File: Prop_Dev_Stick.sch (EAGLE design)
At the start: 54 parts, among them J1 MF-CON-MICROUSB-RIGHT, J3 M20-7822046, J4 M20-7822046, J5 M20-7820442, J6 M20-7820442, U1 P8X32A-Q44, U2 FT230XQ-R, U3 TPS2113ADRBR, U4 CAT24C512WI-GT3, U5 AD7999YRJZ-1500RL7, U6 TS2937CW33, U7 IRLML6401TRPBF, X1 ATS060CSM-1

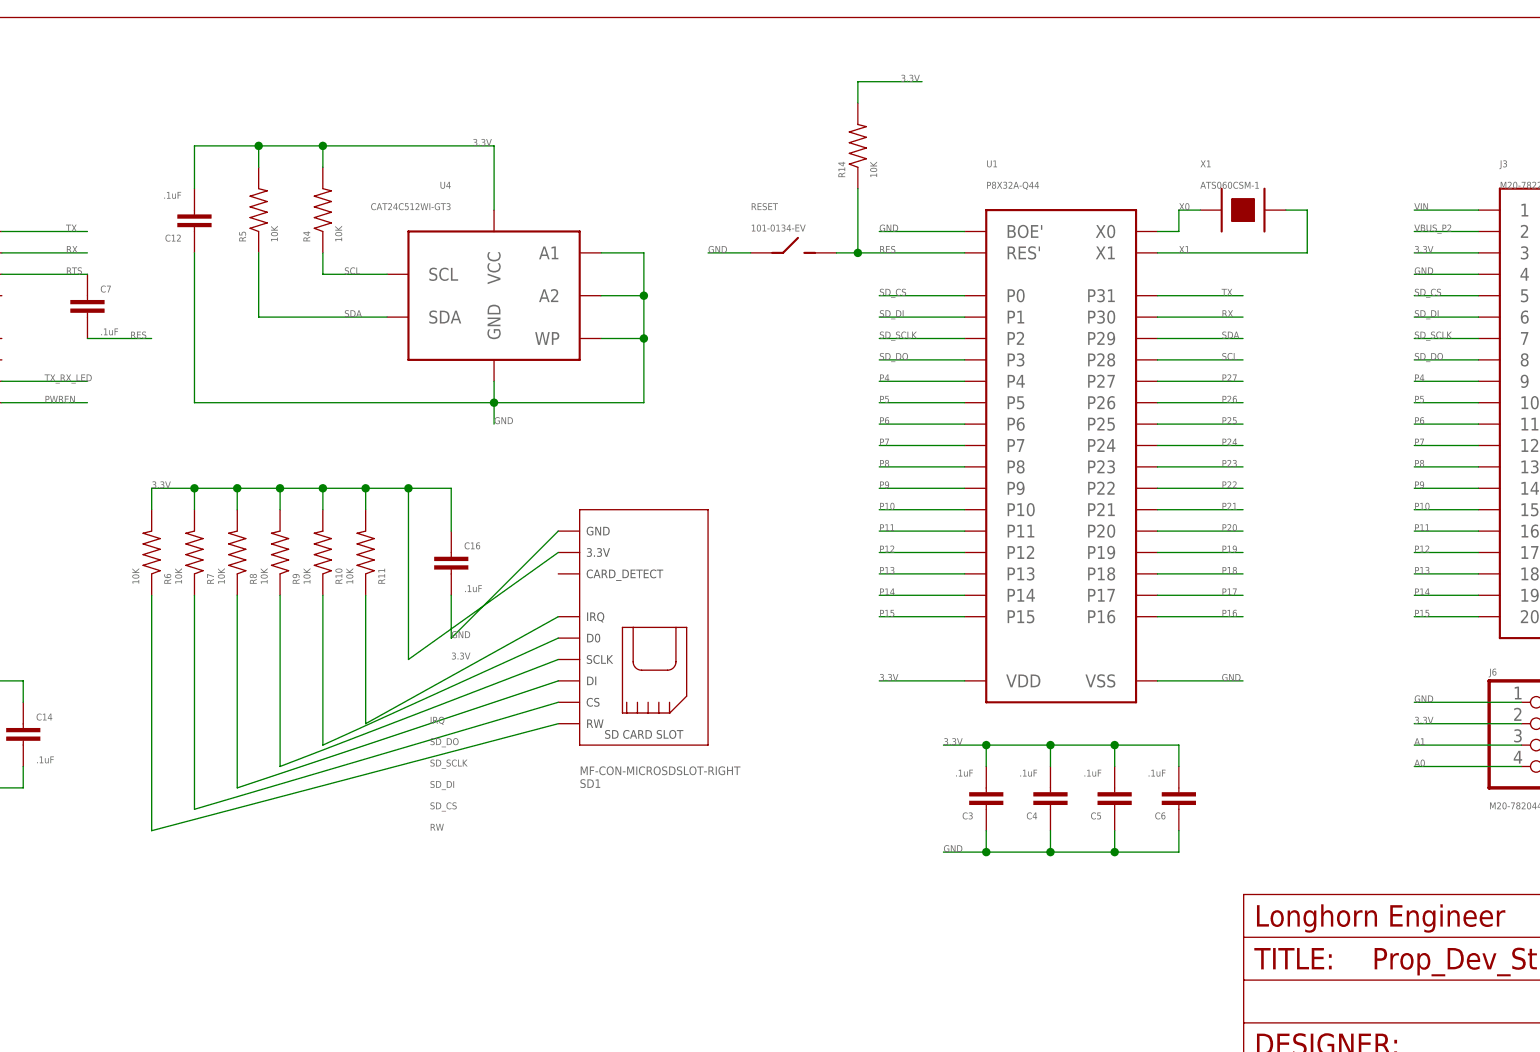
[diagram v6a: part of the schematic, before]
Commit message: Changed crystal.
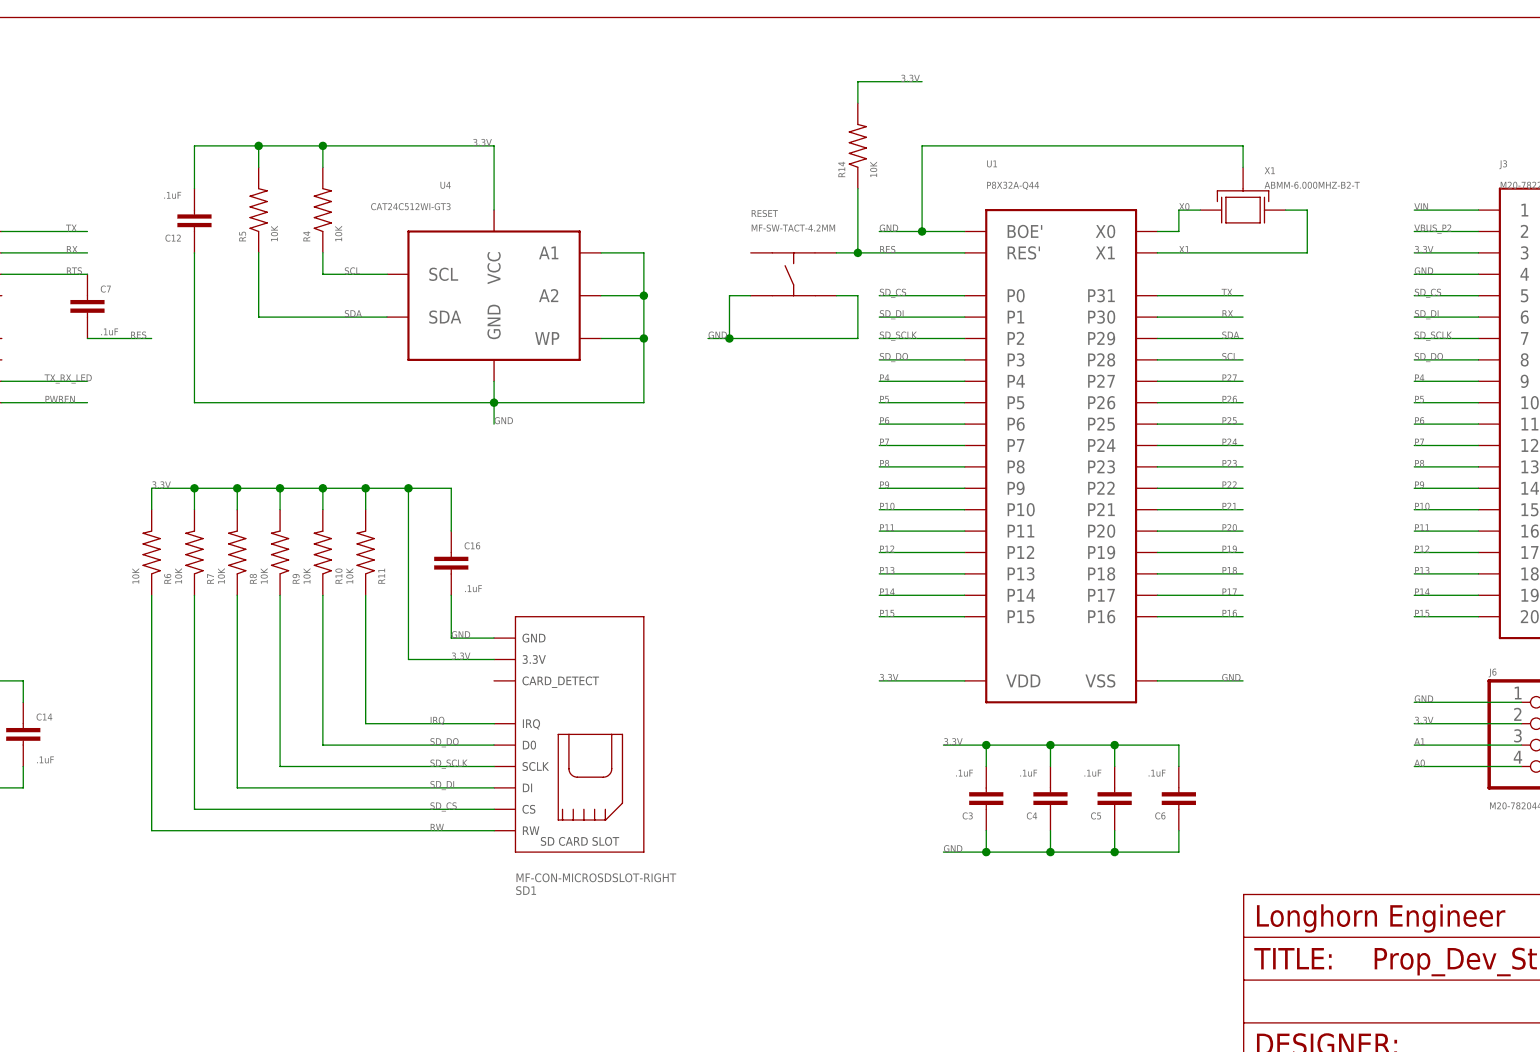
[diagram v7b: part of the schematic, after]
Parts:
- RESET: value 101-0134-EV -> MF-SW-TACT-4.2MM; device PP_Electromechanical:SPST101-0134-EV -> MF_Switches:TACT_4.2MM
- X1: value ATS060CSM-1 -> ABMM-6.000MHZ-B2-T; device PP_FreqCtrl:CRYSTALHC-49 -> MF_Frequency_Control:XTL_7MMX5MM
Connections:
- net GND: now also RESET.P$3, RESET.P$4, X1.GND; no longer RESET.A
- net RES: now also RESET.P$2; no longer RESET.B
- net X0: now also X1.X1; no longer X1.P$1
- net X1: now also X1.X0; no longer X1.P$2
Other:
- moved on the sheet: SD1
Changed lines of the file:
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@@
 <attribute name="REVNUM" value="REV 4"/>
 </part>
-<part name="X1" library="PP_FreqCtrl" deviceset="CRYSTAL" device="HC-49" value="ATS060CSM-1"/>
 <part name="U2" library="PP_DigitalIC" deviceset="FT230X" device="QFN-16" value="FT230XQ-R"/>
 <part name="C1" library="PP_Passives" deviceset="CAPACITOR_NON_POLAR" device="0603" value=".1uF"/>
@@
 <part name="C6" library="PP_Passives" deviceset="CAPACITOR_NON_POLAR" device="0603" value=".1uF"/>
 <part name="C7" library="PP_Passives" deviceset="CAPACITOR_NON_POLAR" device="0603" value=".1uF"/>
-<part name="RESET" library="PP_Electromechanical" deviceset="SPST" device="101-0134-EV" value="101-0134-EV"/>
 <part name="U4" library="PP_DigitalIC" deviceset="CAT24M01XI-T2" device="SOIC-8_W" value="CAT24C512WI-GT3"/>
 <part name="R4" library="PP_Passives" deviceset="RESISTOR" device="0603" value="10K"/>
@@
 <part name="SD1" library="MF_Connectors" deviceset="SD_CARD_SLOT" device="_MICRO_RIGHT" value="MF-CON-MICROSDSLOT-RIGHT"/>
 <part name="J1" library="MF_Connectors" deviceset="USB_CON_5P" device="RIGHT" value="MF-CON-MICROUSB-RIGHT"/>
+<part name="X1" library="MF_Frequency_Control" deviceset="XTL" device="_7MMX5MM" value="ABMM-6.000MHZ-B2-T"/>
+<part name="RESET" library="MF_Switches" deviceset="TACT" device="_4.2MM" value="MF-SW-TACT-4.2MM"/>
 </parts>
 <sheets>
@@
 <attribute name="REVNUM" x="-144.78" y="147.32" size="1.778" layer="96" display="off"/>
 </instance>
-<instance part="X1" gate="G$1" x="-144.78" y="254"/>
 <instance part="U2" gate="G$1" x="-307.34" y="241.3"/>
 <instance part="C1" gate="G$1" x="-345.44" y="231.14"/>
@@
 <instance part="C6" gate="G$1" x="-152.4" y="182.88" rot="R180"/>
 <instance part="C7" gate="G$1" x="-281.94" y="243.84"/>
-<instance part="RESET" gate="G$1" x="-198.12" y="248.92"/>
 <instance part="U4" gate="G$1" x="-233.68" y="241.3" rot="MR0"/>
 <instance part="R4" gate="G$1" x="-254" y="254" rot="R90"/>
@@
 <instance part="R3" gate="G$1" x="-76.2" y="200.66" rot="R90"/>
 <instance part="R18" gate="G$1" x="-76.2" y="185.42" rot="R90"/>
-<instance part="SD1" gate="G$1" x="-223.52" y="190.5" rot="MR180"/>
+<instance part="SD1" gate="G$1" x="-231.14" y="177.8" rot="MR180"/>
 <instance part="J1" gate="G$1" x="-381" y="251.46"/>
+<instance part="X1" gate="G$1" x="-144.78" y="254" smashed="yes" rot="R180">
+<attribute name="NAME" x="-142.24" y="259.08" size="0.8128" layer="95" font="vector" align="top-left"/>
+<attribute name="VALUE" x="-142.24" y="256.54" size="0.8128" layer="96" font="vector"/>
+</instance>
+<instance part="RESET" gate="G$1" x="-198.12" y="246.38" smashed="yes">
+<attribute name="NAME" x="-203.2" y="254" size="0.8128" layer="95" font="vector" align="top-left"/>
+<attribute name="VALUE" x="-203.2" y="251.46" size="0.8128" layer="96" font="vector"/>
+</instance>
 </instances>
 <busses>
@@
 <segment>
 <pinref part="U1" gate="G$1" pin="BOE'"/>
-<wire x1="-177.8" y1="251.46" x2="-187.96" y2="251.46" width="0.1524" layer="91"/>
+<wire x1="-177.8" y1="251.46" x2="-182.88" y2="251.46" width="0.1524" layer="91"/>
 <label x="-187.96" y="251.46" size="0.8128" layer="95" font="vector"/>
+<pinref part="X1" gate="G$1" pin="GND"/>
+<wire x1="-182.88" y1="251.46" x2="-187.96" y2="251.46" width="0.1524" layer="91"/>
+<wire x1="-144.78" y1="259.08" x2="-144.78" y2="261.62" width="0.1524" layer="91"/>
+<wire x1="-144.78" y1="261.62" x2="-182.88" y2="261.62" width="0.1524" layer="91"/>
+<wire x1="-182.88" y1="261.62" x2="-182.88" y2="251.46" width="0.1524" layer="91"/>
+<junction x="-182.88" y="251.46"/>
 </segment>
 <segment>
@@
 </segment>
 <segment>
-<pinref part="RESET" gate="G$1" pin="A"/>
-<wire x1="-203.2" y1="248.92" x2="-208.28" y2="248.92" width="0.1524" layer="91"/>
-<label x="-208.28" y="248.92" size="0.8128" layer="95" font="vector"/>
+<label x="-208.28" y="238.76" size="0.8128" layer="95" font="vector"/>
+<pinref part="RESET" gate="G$1" pin="P$3"/>
+<wire x1="-205.74" y1="238.76" x2="-205.74" y2="243.84" width="0.1524" layer="91"/>
+<wire x1="-205.74" y1="243.84" x2="-203.2" y2="243.84" width="0.1524" layer="91"/>
+<pinref part="RESET" gate="G$1" pin="P$4"/>
+<wire x1="-193.04" y1="243.84" x2="-190.5" y2="243.84" width="0.1524" layer="91"/>
+<wire x1="-190.5" y1="243.84" x2="-190.5" y2="238.76" width="0.1524" layer="91"/>
+<wire x1="-190.5" y1="238.76" x2="-205.74" y2="238.76" width="0.1524" layer="91"/>
+<wire x1="-205.74" y1="238.76" x2="-208.28" y2="238.76" width="0.1524" layer="91"/>
+<junction x="-205.74" y="238.76"/>
 </segment>
 <segment>
@@
 </segment>
 <segment>
-<wire x1="-226.06" y1="215.9" x2="-238.76" y2="203.2" width="0.1524" layer="91"/>
+<wire x1="-233.68" y1="203.2" x2="-238.76" y2="203.2" width="0.1524" layer="91"/>
 <label x="-238.76" y="203.2" size="0.8128" layer="95" font="vector"/>
 <pinref part="C16" gate="G$1" pin="2"/>
@@
 <wire x1="-177.8" y1="248.92" x2="-190.5" y2="248.92" width="0.1524" layer="91"/>
 <label x="-187.96" y="248.92" size="0.8128" layer="95" font="vector"/>
-<pinref part="RESET" gate="G$1" pin="B"/>
 <pinref part="R14" gate="G$1" pin="1"/>
 <wire x1="-190.5" y1="248.92" x2="-193.04" y2="248.92" width="0.1524" layer="91"/>
 <wire x1="-190.5" y1="256.54" x2="-190.5" y2="248.92" width="0.1524" layer="91"/>
 <junction x="-190.5" y="248.92"/>
+<pinref part="RESET" gate="G$1" pin="P$2"/>
 </segment>
 <segment>
@@
 <wire x1="-248.92" y1="220.98" x2="-243.84" y2="220.98" width="0.1524" layer="91"/>
 <wire x1="-243.84" y1="220.98" x2="-243.84" y2="200.66" width="0.1524" layer="91"/>
-<wire x1="-243.84" y1="200.66" x2="-226.06" y2="213.36" width="0.1524" layer="91"/>
+<wire x1="-243.84" y1="200.66" x2="-233.68" y2="200.66" width="0.1524" layer="91"/>
 <label x="-238.76" y="200.66" size="0.8128" layer="95" font="vector"/>
 <label x="-274.32" y="220.98" size="0.8128" layer="95" font="vector"/>
@@
 <net name="SD_SCLK" class="0">
 <segment>
-<wire x1="-226.06" y1="200.66" x2="-259.08" y2="187.96" width="0.1524" layer="91"/>
+<wire x1="-233.68" y1="187.96" x2="-259.08" y2="187.96" width="0.1524" layer="91"/>
 <label x="-241.3" y="187.96" size="0.8128" layer="95" font="vector"/>
 <pinref part="R9" gate="G$1" pin="1"/>
@@
 <net name="SD_DI" class="0">
 <segment>
-<wire x1="-226.06" y1="198.12" x2="-264.16" y2="185.42" width="0.1524" layer="91"/>
+<wire x1="-233.68" y1="185.42" x2="-264.16" y2="185.42" width="0.1524" layer="91"/>
 <label x="-241.3" y="185.42" size="0.8128" layer="95" font="vector"/>
 <pinref part="R8" gate="G$1" pin="1"/>
@@
 <wire x1="-154.94" y1="251.46" x2="-152.4" y2="251.46" width="0.1524" layer="91"/>
 <wire x1="-152.4" y1="251.46" x2="-152.4" y2="254" width="0.1524" layer="91"/>
-<pinref part="X1" gate="G$1" pin="P$1"/>
 <wire x1="-152.4" y1="254" x2="-149.86" y2="254" width="0.1524" layer="91"/>
 <label x="-152.4" y="254" size="0.8128" layer="95" font="vector"/>
+<pinref part="X1" gate="G$1" pin="X1"/>
 </segment>
 </net>
@@
 <wire x1="-154.94" y1="248.92" x2="-137.16" y2="248.92" width="0.1524" layer="91"/>
 <wire x1="-137.16" y1="248.92" x2="-137.16" y2="254" width="0.1524" layer="91"/>
-<pinref part="X1" gate="G$1" pin="P$2"/>
 <wire x1="-137.16" y1="254" x2="-139.7" y2="254" width="0.1524" layer="91"/>
 <label x="-152.4" y="248.92" size="0.8128" layer="95" font="vector"/>
+<pinref part="X1" gate="G$1" pin="X0"/>
 </segment>
 </net>
@@
 <net name="SD_CS" class="0">
 <segment>
-<wire x1="-226.06" y1="195.58" x2="-269.24" y2="182.88" width="0.1524" layer="91"/>
+<wire x1="-233.68" y1="182.88" x2="-269.24" y2="182.88" width="0.1524" layer="91"/>
 <label x="-241.3" y="182.88" size="0.8128" layer="95" font="vector"/>
 <pinref part="R7" gate="G$1" pin="1"/>
@@
 <net name="IRQ" class="0">
 <segment>
-<wire x1="-226.06" y1="205.74" x2="-248.92" y2="193.04" width="0.1524" layer="91"/>
+<wire x1="-233.68" y1="193.04" x2="-248.92" y2="193.04" width="0.1524" layer="91"/>
 <label x="-241.3" y="193.04" size="0.8128" layer="95" font="vector"/>
 <pinref part="R11" gate="G$1" pin="1"/>
@@
 <net name="RW" class="0">
 <segment>
-<wire x1="-226.06" y1="193.04" x2="-274.32" y2="180.34" width="0.1524" layer="91"/>
+<wire x1="-233.68" y1="180.34" x2="-274.32" y2="180.34" width="0.1524" layer="91"/>
 <label x="-241.3" y="180.34" size="0.8128" layer="95" font="vector"/>
 <pinref part="R6" gate="G$1" pin="1"/>
@@
 <net name="SD_DO" class="0">
 <segment>
-<wire x1="-226.06" y1="203.2" x2="-254" y2="190.5" width="0.1524" layer="91"/>
+<wire x1="-233.68" y1="190.5" x2="-254" y2="190.5" width="0.1524" layer="91"/>
 <label x="-241.3" y="190.5" size="0.8128" layer="95" font="vector"/>
 <pinref part="R10" gate="G$1" pin="1"/>

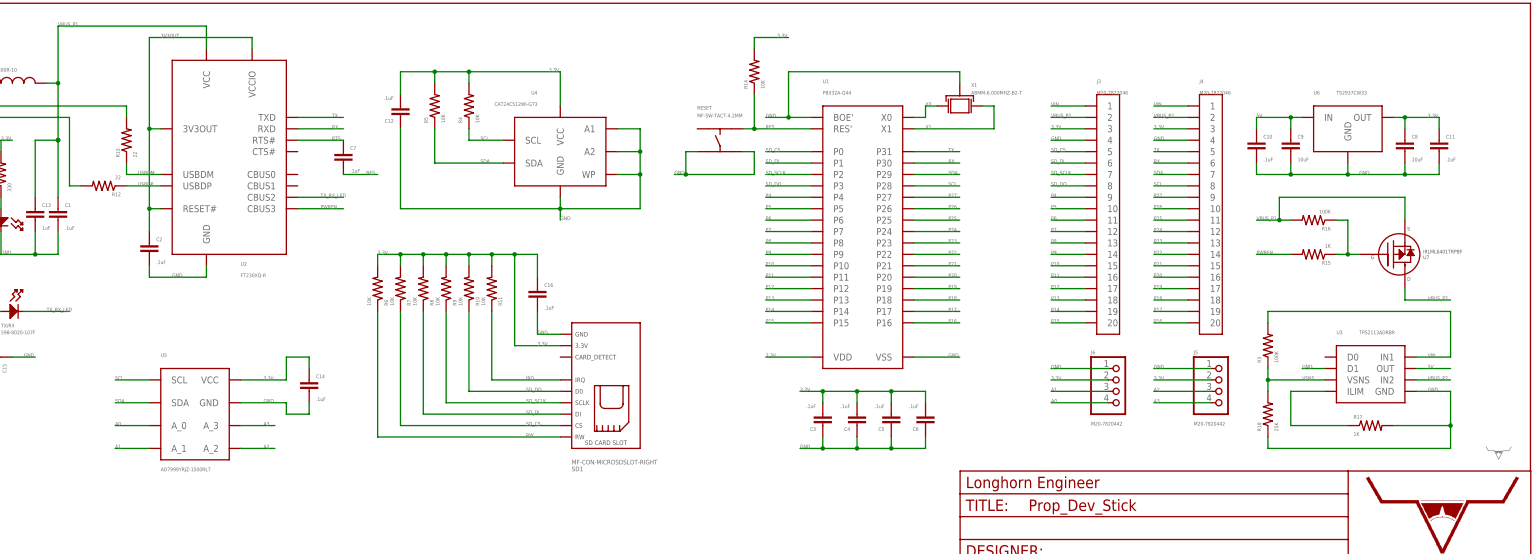
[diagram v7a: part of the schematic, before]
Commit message: REV 4 push
New SD Card, MAX ADC, added 10uF cap.
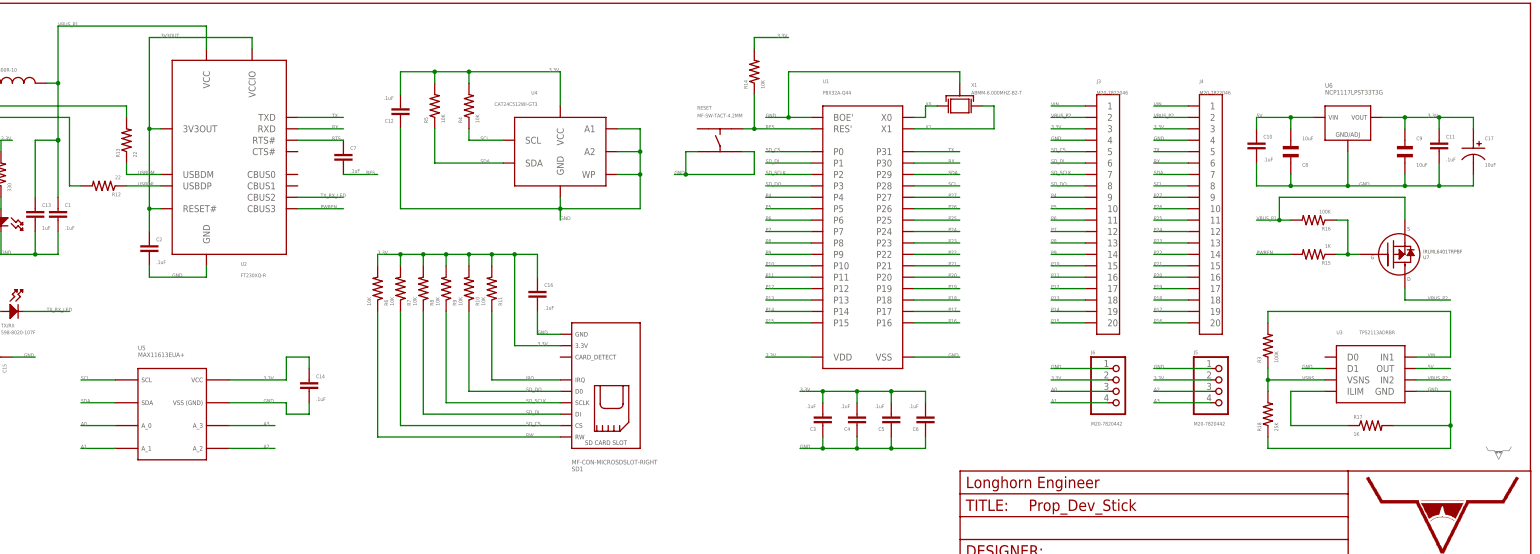
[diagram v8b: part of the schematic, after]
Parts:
- added C17: 10uF, MF_Passives:CAPACITOR_P_4MM
- C8, C9: device PP_Passives:CAPACITOR_NON_POLAR1206 -> MF_Passives:CAPACITOR_NP_1206
- U5: value AD7999YRJZ-1500RL7 -> MAX11613EUA+; device PP_DigitalIC:AD799XSOT-23-8 -> PP_AnalogIC:MAX11613EUA+
- U6: value TS2937CW33 -> NCP1117LPST33T3G; device PP_PowerIC:FIXED_VOLTAGE_REGSOT-223 -> MF_IC_Power:NCP1117LPST33T3G
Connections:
- net 3.3V: now also C17.P$1, C9.P$1, U6.VOUT; no longer C8.1, U6.OUT
- net 5V: now also C8.P$2, U6.VIN; no longer C9.1, U6.IN
- net A0: now also J6.3; no longer J6.4
- net A1: now also J6.4; no longer J6.3
- net GND: now also C17.P$2, C8.P$1, C9.P$2, U6.GND/ADJ; no longer C8.2, C9.2, U6.GND
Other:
- moved on the sheet: C8, C9, U5, U6
